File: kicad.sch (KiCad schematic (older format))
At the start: 8 parts, among them P1 Power, P2 Analog, P3 Digital, P4 Digital, P5 CONN_01X01, P6 CONN_01X01, P7 CONN_01X01, P8 CONN_01X01

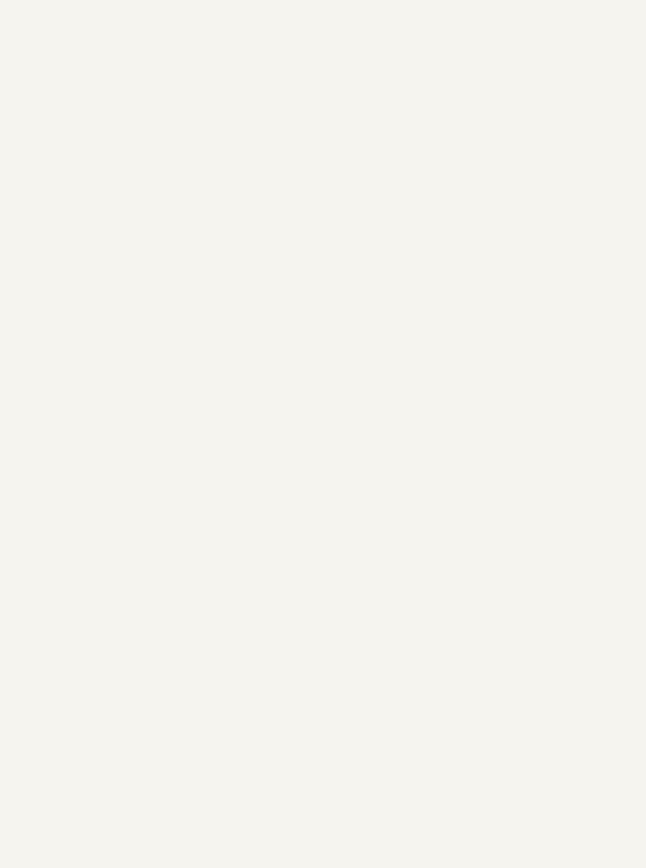
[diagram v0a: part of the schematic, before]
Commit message: Add ATmega328P-PU
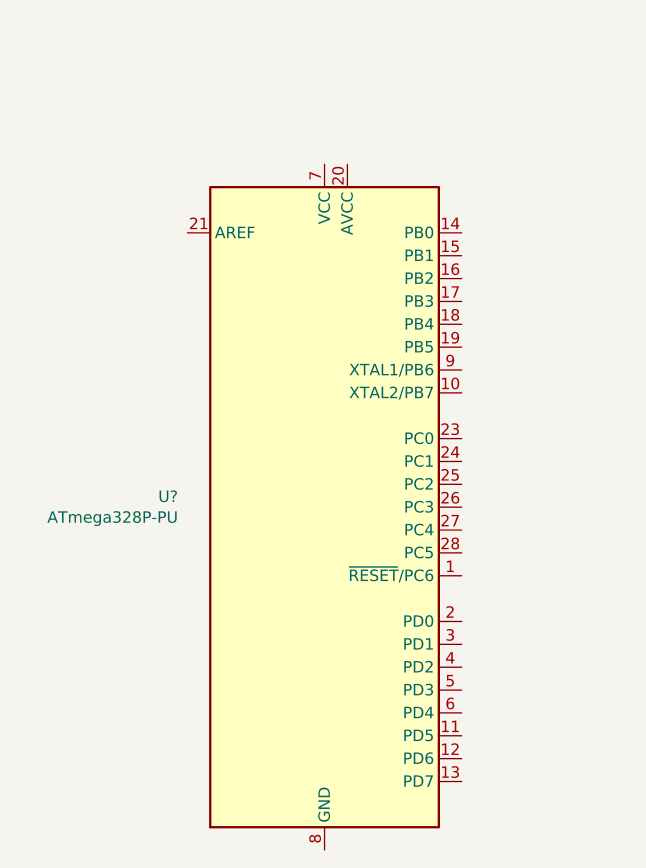
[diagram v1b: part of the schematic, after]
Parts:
- added U?: ATmega328P-PU, Package_DIP:DIP-28_W7.62mm, symbol MCU_Microchip_ATmega:ATmega328P-PU
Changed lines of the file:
@@
 EESchema Schematic File Version 4
-LIBS:Arduino_As_Uno-cache
+LIBS:kicad-cache
 EELAYER 26 0
 EELAYER END
@@
 Wire Notes Line
 	10700 1000 10700 500
+$Comp
+L MCU_Microchip_ATmega:ATmega328P-PU U?
+U 1 1 5BF5C9D7
+P 2900 4050
+F 0 "U?" H 2259 4096 50  0000 R CNN
+F 1 "ATmega328P-PU" H 2259 4005 50  0000 R CNN
+F 2 "Package_DIP:DIP-28_W7.62mm" H 2900 4050 50  0001 C CIN
+F 3 "http://ww1.microchip.com/downloads/en/DeviceDoc/ATmega328_P%20AVR%20MCU%20with%20picoPower%20Technology%20Data%20Sheet%2040001984A.pdf" H 2900 4050 50  0001 C CNN
+	1    2900 4050
+	1    0    0    -1
+$EndComp
 $EndSCHEMATC
